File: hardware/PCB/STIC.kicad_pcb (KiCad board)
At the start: 2 copper layers, 38 x 80 mm, 13 parts, among them IC1 NCP59301DS33R4G, J1 22-03-5035, J2 53047-0510, J3 53047-0310, U1 XIAO_BLE, U2 RM3100_Breakout, U3 MDOB048064AV

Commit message: Update board to show new display, and minor tidying on button board
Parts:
- U3: value MDOB048064AV -> MDOB128064XV; footprint KiCad_imports:MDOB048064AV -> KiCad_imports:MDOB128064XV
- moved J1 8.09 mm to (103.2, 125.8)
- moved U3 7.62 mm to (118.5, 114.5)
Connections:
- U3 pad 1: GND -> +3V3
- U3 pad 2: +3V3 -> GND
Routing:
- net +BATT: track 76.9 -> 69.4 mm
- net +3V3: track 110.6 -> 115.6 mm
- net GND: track 62.4 -> 66.2 mm, vias 3 -> 4
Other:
- outline, holes or cut-outs redrawn
- rule trace_min: 0.5 -> 0.25
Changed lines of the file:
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@@
     (thickness 1.6)
     (drawings 9)
-    (tracks 167)
+    (tracks 169)
     (zones 0)
     (modules 13)
@@
   )
   (setup
-    (last_trace_width 1)
+    (last_trace_width 2)
     (user_trace_width 0.5)
     (user_trace_width 1)
@@
     (zone_clearance 0.508)
     (zone_45_only yes)
-    (trace_min 0.5)
+    (trace_min 0.25)
     (via_size 0.8)
     (via_drill 0.4)
@@
     (add_net "Net-(U2-Pad9)")
   )
+  (module KiCad_imports:MDOB128064XV (layer B.Cu)
+    (at 118.55 114.55 180)
+    (descr "Through hole straight pin header, 1x04, 2.54mm pitch, single row")
+    (tags "Through hole pin header THT 1x04 2.54mm single row")
+    (fp_text reference U3 (at 2.65 3.5 90) (layer B.SilkS)
+      (effects (font (size 1 1) (thickness 0.15)) (justify mirror))
+    )
+    (fp_text value MDOB128064XV (at -0.15 -2.39 180) (layer B.Fab)
+      (effects (font (size 1 1) (thickness 0.15)) (justify mirror))
+    )
+    (fp_line (start -1.7 21.5) (end -1.7 -14) (layer B.CrtYd) (width 0.12))
+    (fp_line (start 30.3 21.5) (end -1.7 21.5) (layer B.CrtYd) (width 0.12))
+    (fp_line (start 30.3 -14) (end 30.3 21.5) (layer B.CrtYd) (width 0.12))
+    (fp_line (start -1.7 -14) (end 30.3 -14) (layer B.CrtYd) (width 0.12))
+    (fp_line (start -1.7 21.5) (end -1.7 -14) (layer B.SilkS) (width 0.12))
+    (fp_line (start 30.3 21.5) (end -1.7 21.5) (layer B.SilkS) (width 0.12))
+    (fp_line (start 30.3 -14) (end 30.3 21.5) (layer B.SilkS) (width 0.12))
+    (fp_line (start -1.7 -14) (end 30.3 -14) (layer B.SilkS) (width 0.12))
+    (fp_line (start -0.785 8.83) (end 1.12 8.83) (layer B.Fab) (width 0.1))
+    (fp_line (start 1.12 8.83) (end 1.12 -1.33) (layer B.Fab) (width 0.1))
+    (fp_line (start 1.12 -1.33) (end -1.42 -1.33) (layer B.Fab) (width 0.1))
+    (fp_line (start -1.42 -1.33) (end -1.42 8.195) (layer B.Fab) (width 0.1))
+    (fp_line (start -1.42 8.195) (end -0.785 8.83) (layer B.Fab) (width 0.1))
+    (fp_text user %R (at -0.15 3.75 90) (layer B.Fab)
+      (effects (font (size 1 1) (thickness 0.15)) (justify mirror))
+    )
+    (pad 4 thru_hole circle (at -0.15 7.56 180) (size 1.7 1.7) (drill 1) (layers *.Cu *.Mask)
+      (net 12 /SDA))
+    (pad 3 thru_hole oval (at -0.15 5.02 180) (size 1.7 1.7) (drill 1) (layers *.Cu *.Mask)
+      (net 13 /SCL))
+    (pad 2 thru_hole oval (at -0.15 2.48 180) (size 1.7 1.7) (drill 1) (layers *.Cu *.Mask)
+      (net 1 GND))
+    (pad 1 thru_hole rect (at -0.15 -0.06 180) (size 1.7 1.7) (drill 1) (layers *.Cu *.Mask)
+      (net 4 +3V3))
+    (model ${KICAD_USER_TEMPLATE_DIR}/MDOB128064XV.step
+      (offset (xyz 30.3 -14 1.5))
+      (scale (xyz 1 1 1))
+      (rotate (xyz 0 0 -90))
+    )
+  )
   (module Capacitor_THT:C_Rect_L7.2mm_W5.5mm_P5.00mm_FKS2_FKP2_MKS2_MKP2 (layer F.Cu)
     (at 114.434 121.154 270)
@@
   )
   (module Connector_Molex:Molex_SPOX_5267-03A_1x03_P2.50mm_Vertical (layer F.Cu)
-    (at 101.95 133.75)
+    (at 103.15 125.75)
     (descr "Molex SPOX Connector System, 5267-03A, 3 Pins per row (http://www.molex.com/pdm_docs/sd/022035035_sd.pdf), generated with kicad-footprint-generator")
     (tags "connector Molex SPOX side entry")
@@
     )
   )
-  (module KiCad_imports:MDOB048064AV (layer B.Cu)
-    (at 118.752 106.93 180)
-    (descr "Through hole straight pin header, 1x04, 2.54mm pitch, single row")
-    (tags "Through hole pin header THT 1x04 2.54mm single row")
-    (fp_text reference U3 (at 2.8 -4.06 90) (layer B.SilkS)
-      (effects (font (size 1 1) (thickness 0.15)) (justify mirror))
-    )
-    (fp_text value MDOB048064AV (at 0 -9.95 180) (layer B.Fab)
-      (effects (font (size 1 1) (thickness 0.15)) (justify mirror))
-    )
-    (fp_line (start -0.635 1.27) (end 1.27 1.27) (layer B.Fab) (width 0.1))
-    (fp_line (start 1.27 1.27) (end 1.27 -8.89) (layer B.Fab) (width 0.1))
-    (fp_line (start 1.27 -8.89) (end -1.27 -8.89) (layer B.Fab) (width 0.1))
-    (fp_line (start -1.27 -8.89) (end -1.27 0.635) (layer B.Fab) (width 0.1))
-    (fp_line (start -1.27 0.635) (end -0.635 1.27) (layer B.Fab) (width 0.1))
-    (fp_text user %R (at 0 -3.81) (layer B.Fab)
-      (effects (font (size 1 1) (thickness 0.15)) (justify mirror))
-    )
-    (fp_line (start -1.5 4.14) (end -1.5 -11.76) (layer B.SilkS) (width 0.12))
-    (fp_line (start -1.5 -11.76) (end 25.5 -11.76) (layer B.SilkS) (width 0.12))
-    (fp_line (start 25.5 -11.76) (end 25.5 4.14) (layer B.SilkS) (width 0.12))
-    (fp_line (start 25.5 4.14) (end -1.5 4.14) (layer B.SilkS) (width 0.12))
-    (fp_line (start -1.5 4.14) (end 25.5 4.14) (layer B.CrtYd) (width 0.12))
-    (fp_line (start 25.5 4.14) (end 25.5 -11.76) (layer B.CrtYd) (width 0.12))
-    (fp_line (start 25.5 -11.76) (end -1.5 -11.76) (layer B.CrtYd) (width 0.12))
-    (fp_line (start -1.5 -11.76) (end -1.5 4.14) (layer B.CrtYd) (width 0.12))
-    (pad 4 thru_hole circle (at 0 0 180) (size 1.7 1.7) (drill 1) (layers *.Cu *.Mask)
-      (net 12 /SDA))
-    (pad 3 thru_hole oval (at 0 -2.54 180) (size 1.7 1.7) (drill 1) (layers *.Cu *.Mask)
-      (net 13 /SCL))
-    (pad 2 thru_hole oval (at 0 -5.08 180) (size 1.7 1.7) (drill 1) (layers *.Cu *.Mask)
-      (net 4 +3V3))
-    (pad 1 thru_hole rect (at 0 -7.62 180) (size 1.7 1.7) (drill 1) (layers *.Cu *.Mask)
-      (net 1 GND))
-    (model ${KICAD_USER_TEMPLATE_DIR}/MDOB048064AV.step
-      (at (xyz 0 0 0))
-      (scale (xyz 1 1 1))
-      (rotate (xyz 0 0 0))
-    )
-  )
   (module Resistor_THT:R_Axial_DIN0207_L6.3mm_D2.5mm_P7.62mm_Horizontal (layer F.Cu)
     (at 119.26 99.31 90)
@@
     )
   )
-  (gr_circle (center 103.766 125.218) (end 104.496 123.898) (layer Edge.Cuts) (width 0.05))
+  (gr_circle (center 103.641591 133.45) (end 104.371591 132.13) (layer Edge.Cuts) (width 0.05))
   (gr_line (start 84.75 136.75) (end 84.75 60.75) (layer Edge.Cuts) (width 0.05))
   (gr_line (start 86.75 138.75) (end 84.75 136.75) (layer Edge.Cuts) (width 0.05))
@@
   (segment (start 114.434 126.934) (end 114.434 126.154) (width 1) (layer F.Cu) (net 1))
   (segment (start 117.65 130.15) (end 114.434 126.934) (width 1) (layer F.Cu) (net 1))
+  (segment (start 118.7 112.07) (end 114.97 112.07) (width 1) (layer F.Cu) (net 1))
+  (segment (start 114.97 112.07) (end 114.97 112.07) (width 1) (layer F.Cu) (net 1))
+  (via (at 114.97 112.07) (size 2) (drill 1) (layers F.Cu B.Cu) (net 1))
   (segment (start 94.75 65.95218) (end 88.95218 65.95218) (width 1) (layer F.Cu) (net 2))
   (via (at 88.95218 65.95218) (size 2) (drill 1) (layers F.Cu B.Cu) (net 2))
@@
   (segment (start 103.18 119.88) (end 103.18 116.261) (width 1) (layer F.Cu) (net 4))
   (segment (start 104.454 121.154) (end 103.18 119.88) (width 1) (layer F.Cu) (net 4))
-  (segment (start 114.434 121.154) (end 114.434 114.866) (width 1) (layer F.Cu) (net 4))
-  (segment (start 114.434 114.866) (end 117.29 112.01) (width 1) (layer F.Cu) (net 4))
   (segment (start 115.19 95.24) (end 119.26 99.31) (width 1) (layer B.Cu) (net 4))
   (segment (start 115.19 93.69) (end 115.19 95.24) (width 1) (layer B.Cu) (net 4))
-  (segment (start 117.81 112.01) (end 116.21 112.01) (width 1) (layer F.Cu) (net 4))
-  (segment (start 117.29 112.01) (end 117.81 112.01) (width 1) (layer F.Cu) (net 4))
-  (segment (start 117.81 112.01) (end 118.752 112.01) (width 1) (layer F.Cu) (net 4))
-  (segment (start 113.55 109.35) (end 113.55 99.75) (width 1) (layer F.Cu) (net 4))
-  (segment (start 116.21 112.01) (end 113.55 109.35) (width 1) (layer F.Cu) (net 4))
   (segment (start 113.55 99.75) (end 114.21 99.69) (width 1) (layer F.Cu) (net 4))
   (segment (start 108.592 99.69) (end 113.55 99.75) (width 1) (layer F.Cu) (net 4))
+  (segment (start 114.434 121.154) (end 114.434 118.166) (width 1) (layer F.Cu) (net 4))
+  (segment (start 117.99 114.61) (end 118.7 114.61) (width 1) (layer F.Cu) (net 4))
+  (segment (start 114.434 118.166) (end 117.99 114.61) (width 1) (layer F.Cu) (net 4))
+  (segment (start 114.434 121.154) (end 114.434 117.534) (width 1) (layer F.Cu) (net 4))
+  (segment (start 114.434 117.534) (end 112.05 115.15) (width 1) (layer F.Cu) (net 4))
+  (segment (start 112.05 101.25) (end 113.55 99.75) (width 1) (layer F.Cu) (net 4))
+  (segment (start 112.05 115.15) (end 112.05 101.25) (width 1) (layer F.Cu) (net 4))
   (segment (start 112.678 80.514) (end 110.178 80.514) (width 1) (layer B.Cu) (net 5))
   (segment (start 115.05737 80.514) (end 112.678 80.514) (width 1) (layer B.Cu) (net 5))
@@
   (segment (start 115.75 108.25) (end 116.97 109.47) (width 1) (layer F.Cu) (net 13))
   (via (at 99.75 71.25) (size 3) (drill 2) (layers F.Cu B.Cu) (net 16) (status 30))
-  (segment (start 101.95 133.75) (end 101.95 131.75) (width 2) (layer B.Cu) (net 16))
-  (segment (start 98.686 128.486) (end 98.686 121.408) (width 2) (layer B.Cu) (net 16))
-  (segment (start 101.95 131.75) (end 98.686 128.486) (width 2) (layer B.Cu) (net 16))
   (segment (start 99.78 120.314) (end 98.686 121.408) (width 1) (layer F.Cu) (net 16))
   (segment (start 99.78 116.261) (end 99.78 120.314) (width 1) (layer F.Cu) (net 16))
@@
   (segment (start 103.75 75.25) (end 99.75 71.25) (width 2) (layer B.Cu) (net 16))
   (segment (start 103.75 82.25) (end 103.75 75.25) (width 2) (layer B.Cu) (net 16))
+  (segment (start 103.028 125.75) (end 98.686 121.408) (width 2) (layer B.Cu) (net 16))
+  (segment (start 103.15 125.75) (end 103.028 125.75) (width 2) (layer B.Cu) (net 16))
   (segment (start 90.324 134.108) (end 90.324 132.424) (width 1) (layer B.Cu) (net 19))
   (segment (start 90.324 132.424) (end 86.35 128.45) (width 1) (layer B.Cu) (net 19))

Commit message: Add battery charger IC and switch caps to SMT tech
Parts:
- removed R1: 1k, Resistor_THT:R_Axial_DIN0207_L6.3mm_D2.5mm_P7.62mm_Horizontal
- U3: value MDOB128064XV -> OLED1_3_GND1; footprint KiCad_imports:MDOB128064XV -> KiCad_imports:OLED1_3
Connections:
- LS1 pad 2: Net-(LS1-Pad2) -> /BUZZER_A
- U3 pad 1: +3V3 -> GND
- U3 pad 2: GND -> +3V3
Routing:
- net Net-(LS1-Pad2): track 12.0 -> 0.00 mm
- net GND: track 66.2 -> 75.9 mm, vias 4 -> 3
- net /BUZZER_A: track 11.9 -> 17.9 mm, vias 0 -> 1
- net +3V3: track 115.6 -> 115.1 mm

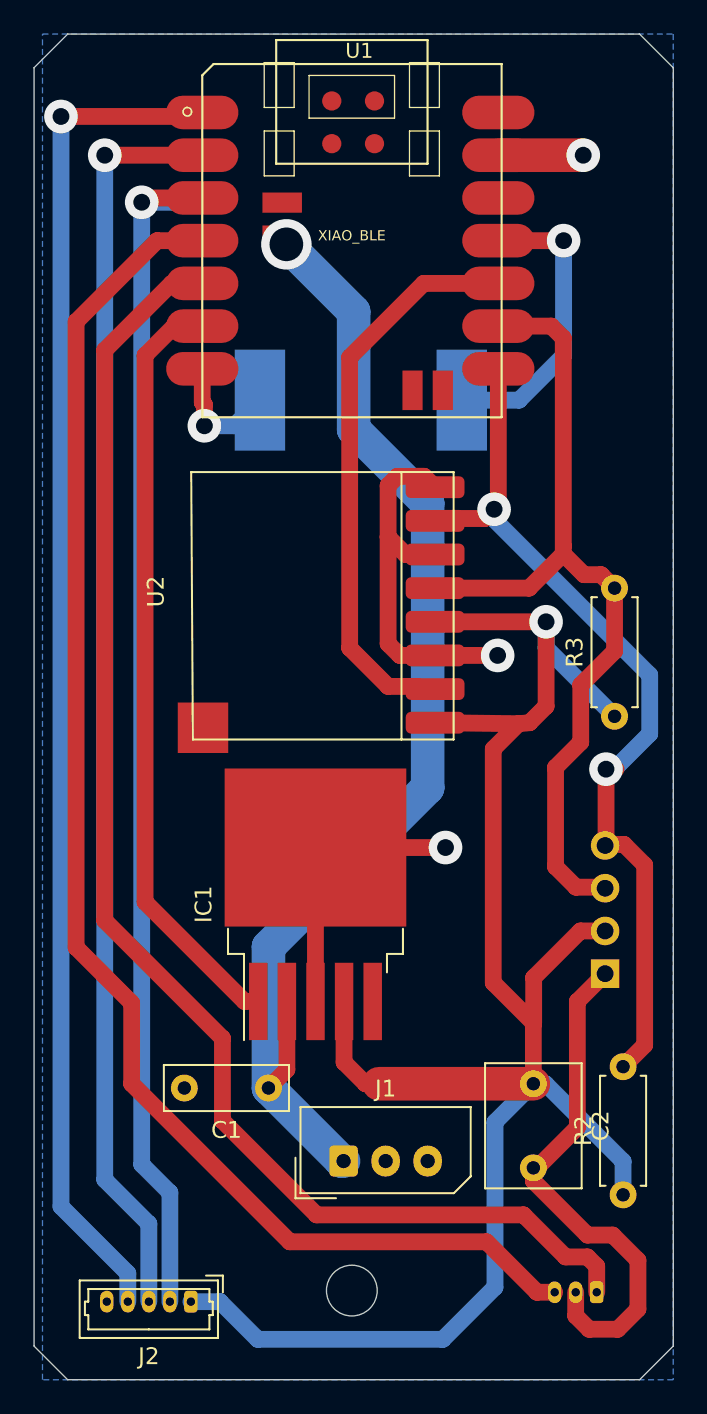
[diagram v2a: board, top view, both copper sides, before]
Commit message: Update pcb to include battery charging and smaller current controller
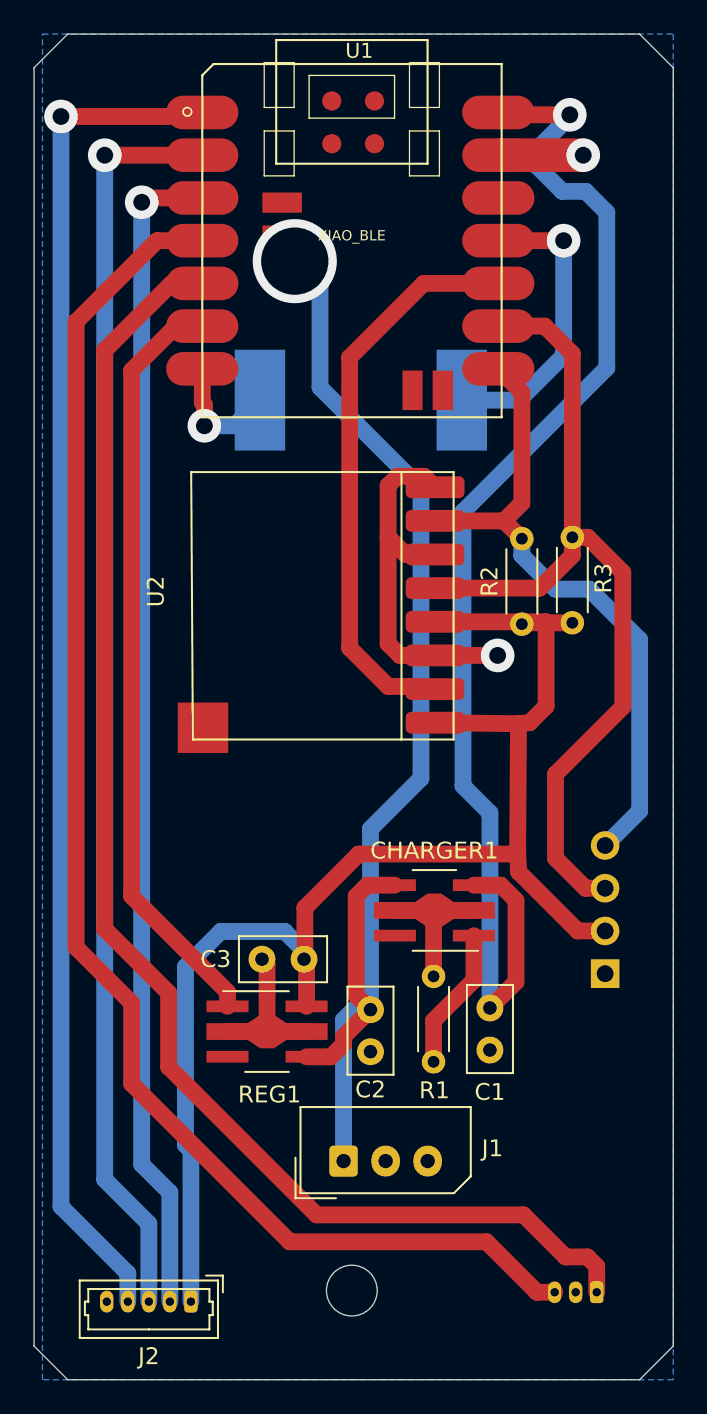
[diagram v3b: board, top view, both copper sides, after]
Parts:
- removed IC1: NCP59301DS33R4G, Package_TO_SOT_SMD:TO-263-5_TabPin6
- added C3: 4.7uF, Capacitor_THT:C_Disc_D5.0mm_W2.5mm_P2.50mm, F.Cu at (100.8, 113.8)
- added CHARGER1: XC6802A42XMR-G, Package_TO_SOT_SMD:SOT-89-5_Handsoldering, F.Cu at (108.5, 110.8)
- added R1: 2k, Resistor_THT:R_Axial_DIN0204_L3.6mm_D1.6mm_P5.08mm_Horizontal, F.Cu at (108.5, 119.8)
- added REG1: AP7361C-33Y5-13, Package_TO_SOT_SMD:SOT-89-5_Handsoldering, F.Cu at (98.6, 118.0)
- C1: value 1uF -> 1.0uF; footprint Capacitor_THT:C_Rect_L7.2mm_W2.5mm_P5.00mm_FKS2_FKP2_MKS2_MKP2 -> Capacitor_THT:C_Disc_D5.0mm_W2.5mm_P2.50mm
- C2: value 47uF -> 1.0uF; footprint Capacitor_THT:C_Rect_L7.2mm_W5.5mm_P5.00mm_FKS2_FKP2_MKS2_MKP2 -> Capacitor_THT:C_Disc_D5.0mm_W2.5mm_P2.50mm
- R2, R3: value 10k -> 2k; footprint Resistor_THT:R_Axial_DIN0207_L6.3mm_D2.5mm_P7.62mm_Horizontal -> Resistor_THT:R_Axial_DIN0204_L3.6mm_D1.6mm_P5.08mm_Horizontal
- moved R2 34.5 mm to (113.8, 93.8)
- moved C1 14.0 mm to (111.8, 116.7), turned to 270 degrees
- moved C2 10.6 mm to (104.8, 116.8)
- moved R3 6.10 mm to (116.8, 93.8)
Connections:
- C1 pad 1: +BATT -> VBUS
- C2 pad 1: +3V3 -> +BATT
- U1 pad 14: Net-(U1-Pad14) -> VBUS
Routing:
- net VBUS: track 0.00 -> 74.9 mm, vias 0 -> 1
- net GND: track 75.9 -> 45.5 mm, vias 3 -> 2
- net +3V3: track 115.1 -> 86.3 mm, vias 1 -> 0
- net /SDA: track 53.3 -> 38.8 mm, vias 2 -> 0
- net Net-(CHARGER1-Pad1): track 0.00 -> 8.49 mm
- net +BATT: track 69.4 -> 74.7 mm
- net /Tx: track 72.7 -> 69.8 mm
- net /SCL: track 50.9 -> 52.2 mm
- net /PERIPH_EN: track 45.8 -> 46.8 mm
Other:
- board text added: "SAP 6.1"
